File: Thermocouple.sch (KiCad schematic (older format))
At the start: 0 parts

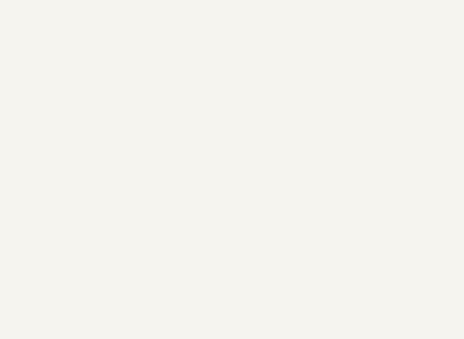
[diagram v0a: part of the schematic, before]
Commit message: Defining Inputs and Outputs
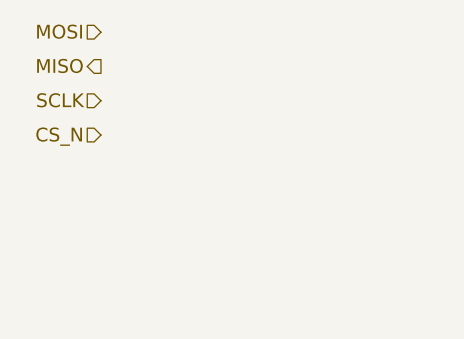
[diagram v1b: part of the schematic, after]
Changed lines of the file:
@@
 Text HLabel 8550 3250 2    60   Input ~ 0
 TC IN -
+Text HLabel 1800 2050 0    60   Input ~ 0
+MOSI
+Text HLabel 1800 2200 0    60   Output ~ 0
+MISO
+Text HLabel 1800 2350 0    60   Input ~ 0
+SCLK
+Text HLabel 1800 2500 0    60   Input ~ 0
+CS_N
 $EndSCHEMATC

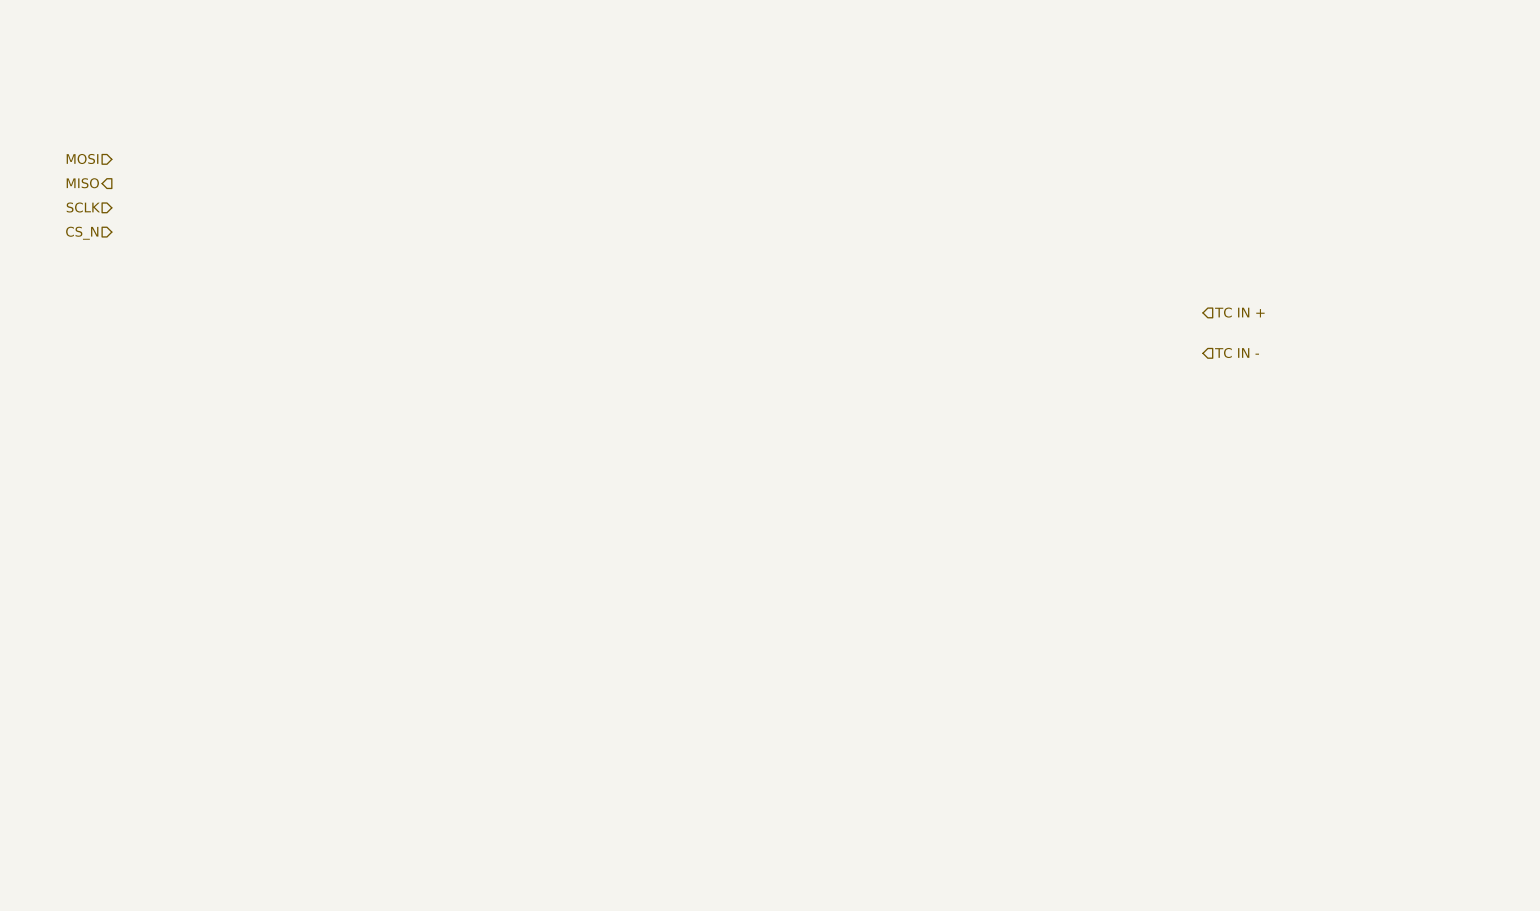
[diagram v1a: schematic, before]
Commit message: Added TC block diagram
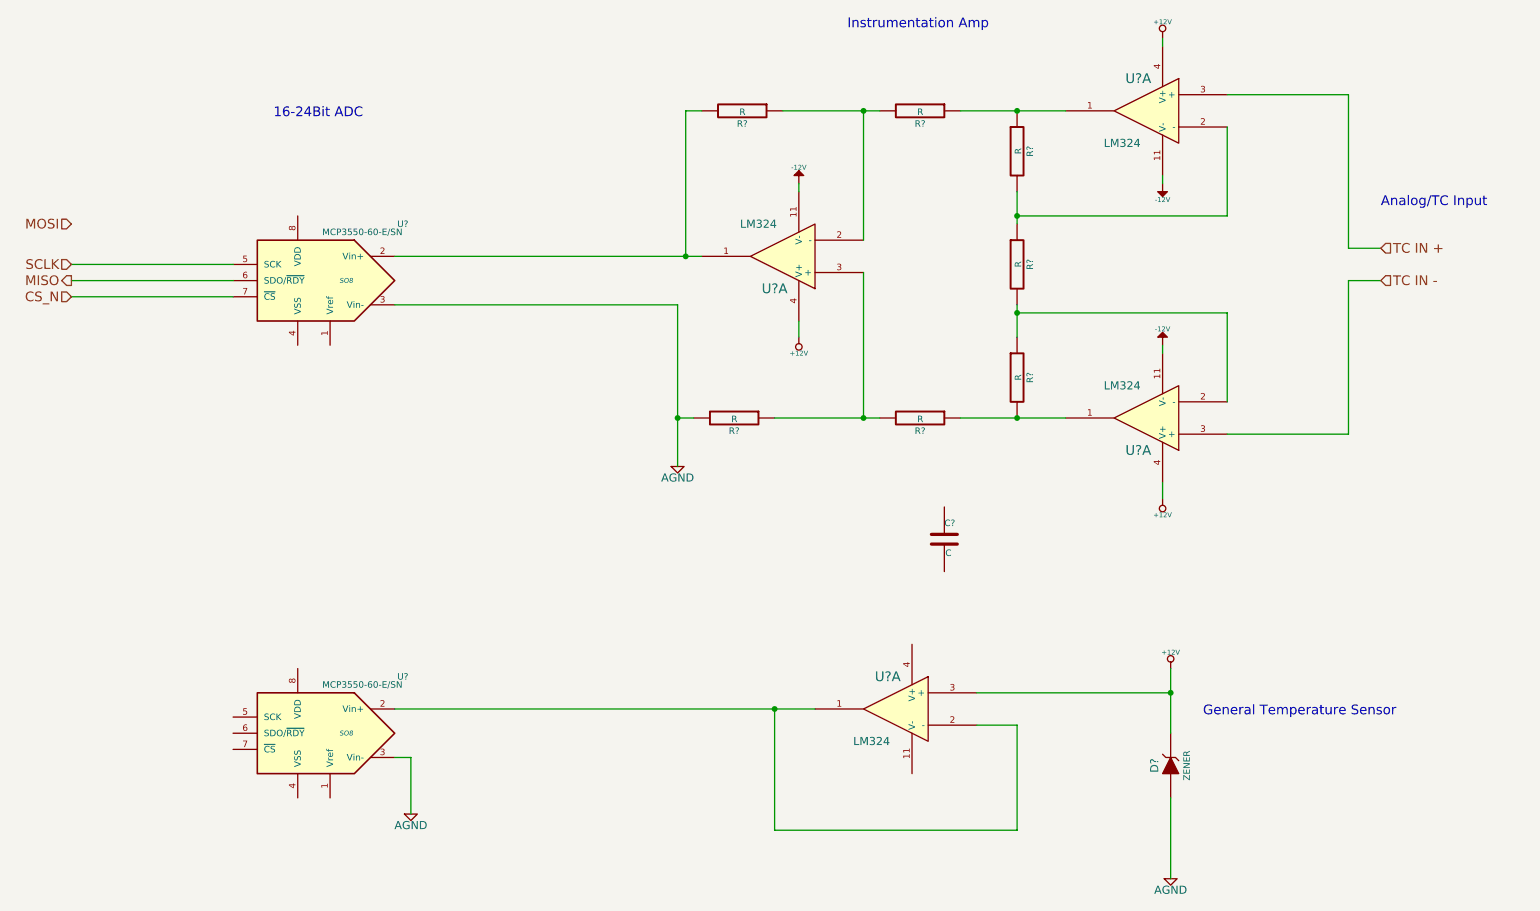
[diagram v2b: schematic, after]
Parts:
- added C?: C, ~, symbol C
- added D?: ZENER, ~, symbol ZENER
- added R? (x7): R, ~, symbol R
- added U? (x4): LM324, symbol LM324
- added U? (x2): MCP3550-60-E/SN, SO8, symbol MCP3550-60-E/SN
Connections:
- net CS_N: now also U?.7 (~CS~)
- net MISO: now also U?.6 (SDO/~RDY~)
- net SCLK: now also U?.5 (SCK)
- net TC IN +: now also U?.3 (+)
- net TC IN -: now also U?.3 (+)
- new net: R?.1, R?.1, U?.1
- new net: R?.1, R?.2, U?.2 (-) (x3)
- new net: R?.1, R?.2, U?.1
- new net: R?.2, U?.1, U?.2 (Vin+)
- new net: R?.1, R?.2, U?.3 (+)
- new net: U?.1, U?.2 (-), U?.2 (Vin+)
- new net +12V: D?.2 (K), U?.3 (+), U?.4 (V+), U?.4 (V+), U?.4 (V+)
- new net -12V: U?.11 (V-), U?.11 (V-), U?.11 (V-)
- new net AGND: D?.1 (A), R?.2, U?.3 (Vin-), U?.3 (Vin-)
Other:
- note added: "16-24Bit ADC"
- note added: "Analog/TC Input"
- note added: "General Temperature Sensor"
- note added: "Instrumentation Amp"
